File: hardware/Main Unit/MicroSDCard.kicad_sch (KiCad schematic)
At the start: 18 parts, among them J10 DM3AT, U7 74AHC1G04, U8 AP22913W6-7, U9 SN74AXC4T774

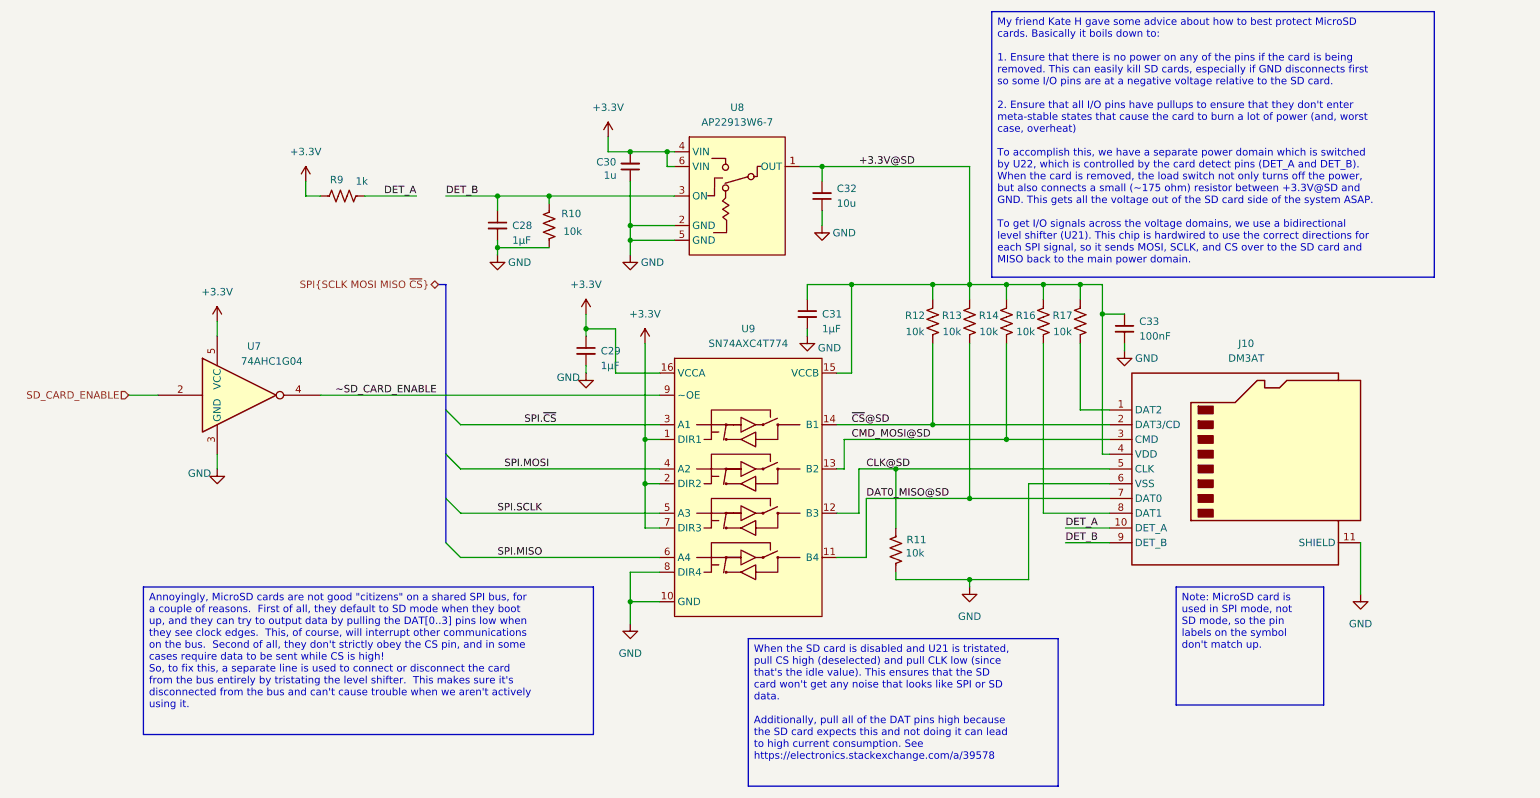
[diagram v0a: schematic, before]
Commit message: Implement Ethernet, start on voltage regulator
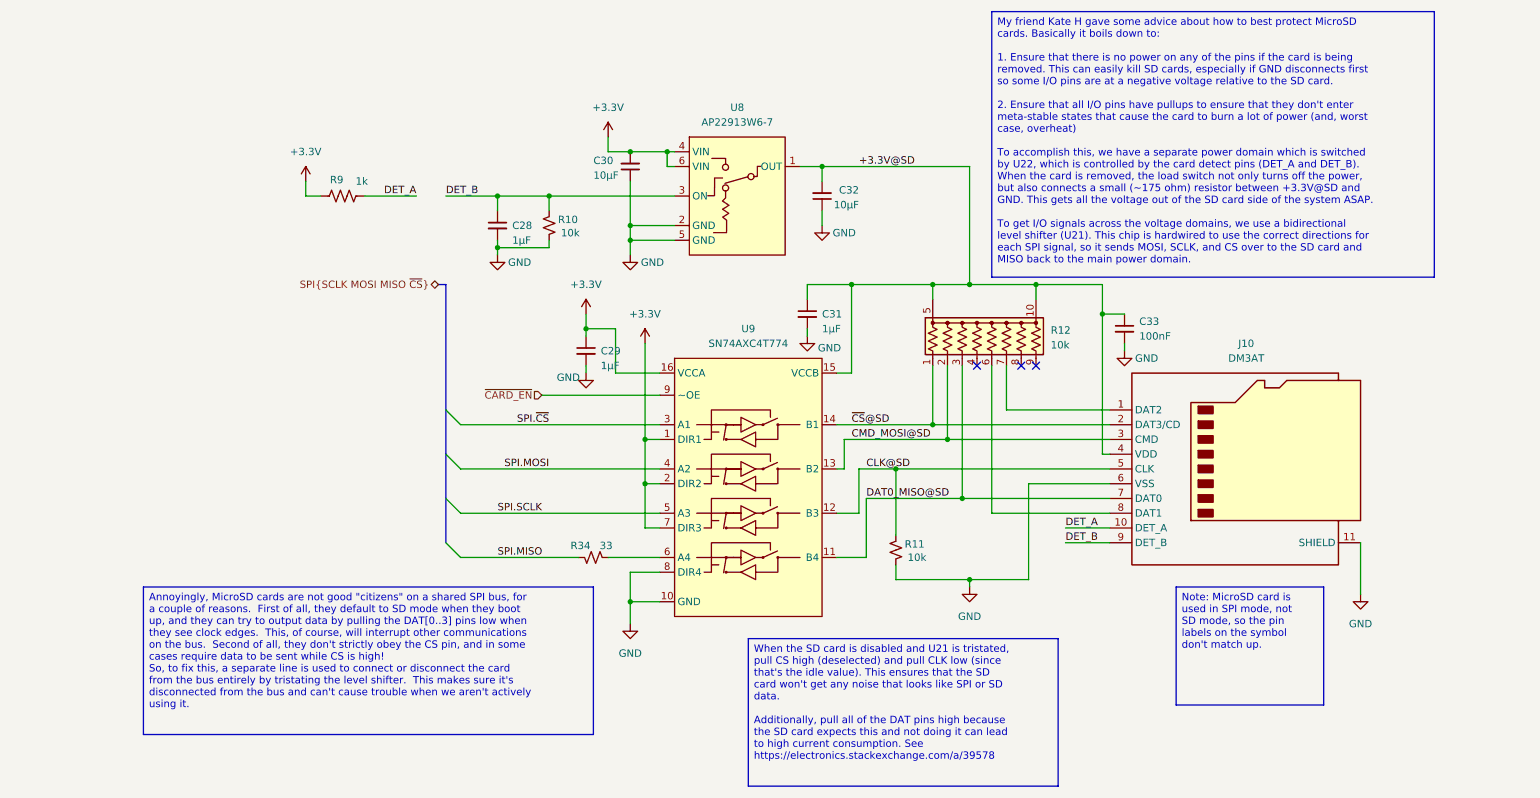
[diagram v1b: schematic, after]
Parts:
- removed R10, R11, R12, R13, R14, R16, R17: 10k, Resistor_SMD:R_1206_3216Metric, symbol Device:R_US
- removed U7: 74AHC1G04, Package_TO_SOT_SMD:SOT-23-5, symbol 74xGxx:74AHC1G04
- added R10, R11: 10k, Resistor_SMD:R_0603_1608Metric, symbol Device:R_Small_US
- added R12: 10k, Project Library:CTS 745C101, symbol Project Library:CTS 745C101
- added R34: 33, Resistor_SMD:R_0603_1608Metric, symbol Device:R_Small_US
- C30: value 1u -> 10µF; LibRef CL31B105KBHNNNE -> CL31B106KLHNNNE
- C32: value 10u -> 10µF
- U8: symbol project libraries:AP22913W6-7 -> Project Library:AP22913W6-7
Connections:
- net +3.3V@SD: now also R12.10 (common), R12.5 (common)
- net CLK@SD: now also R11.2
- net CMD_MOSI@SD: now also R12.2 (R2)
- net DAT0_MISO@SD: now also R12.3 (R3)
- net DET_B: now also R10.2
- net GND: now also R10.1, R11.1
- net SPI.MISO: now also R34.1; no longer U9.6 (A4)
- net ~{CS}@SD: now also R12.1 (R1)
- net at J10.8 (DAT1): now also R12.6 (R5)
- net at J10.1 (DAT2): now also R12.7 (R6)
- net ~SD_CARD_ENABLE renamed ~{CARD_EN}
- new net: R34.2, U9.6 (A4)
- no-connect marks 0 -> 3

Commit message: Main unit: Add USB port for MCU and 3.3VA rail, start on routing
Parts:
- U9: symbol project libraries:SN74AXC4T774 -> Project Library:SN74AXC4T774
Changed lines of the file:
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@@
 	)
 	(symbol
-		(lib_id "project libraries:SN74AXC4T774")
+		(lib_id "Project Library:SN74AXC4T774")
 		(at 140.97 93.98 0)
 		(unit 1)

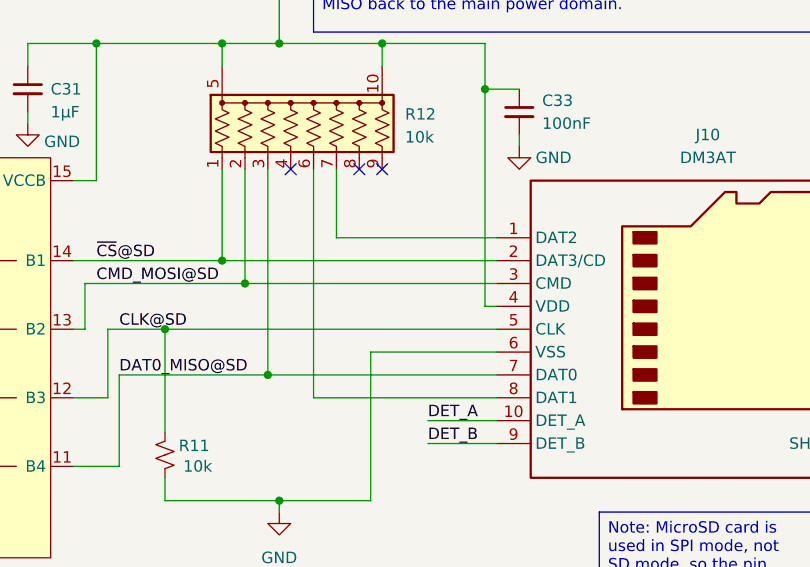
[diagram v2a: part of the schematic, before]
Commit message: Route most of the data lines on the PCB
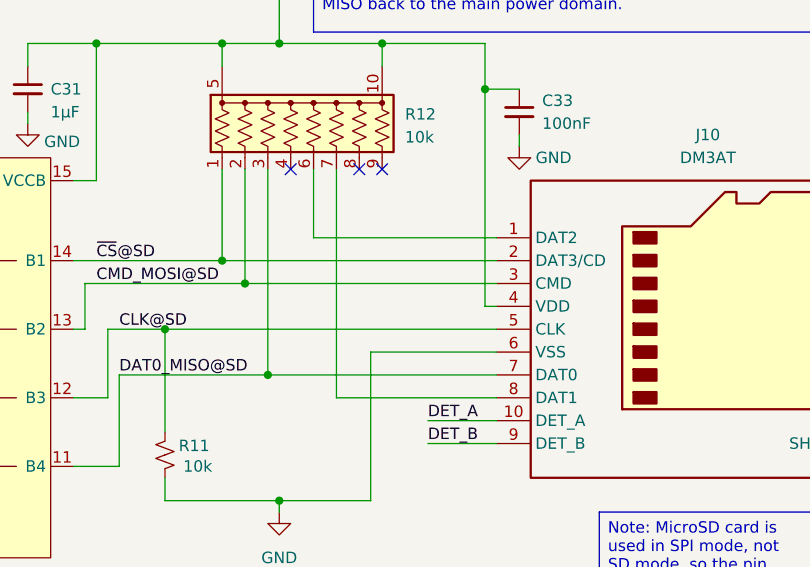
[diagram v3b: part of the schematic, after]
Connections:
- net at R12.6 (R5): now also J10.1 (DAT2); no longer J10.8 (DAT1)
- net at R12.7 (R6): now also J10.8 (DAT1); no longer J10.1 (DAT2)
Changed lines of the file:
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@@
-	(wire
-		(pts
-			(xy 182.88 101.6) (xy 203.2 101.6)
-		)
-		(stroke
-			(width 0)
-			(type default)
-		)
-	)
 	(wire
 		(pts
@@
 	(wire
 		(pts
+			(xy 185.42 76.2) (xy 185.42 101.6)
+		)
+		(stroke
+			(width 0)
+			(type default)
+		)
+	)
+	(wire
+		(pts
 			(xy 205.74 72.39) (xy 205.74 73.66)
 		)
@@
 	(wire
 		(pts
-			(xy 182.88 101.6) (xy 182.88 76.2)
-		)
-		(stroke
-			(width 0)
-			(type default)
-		)
-	)
-	(wire
-		(pts
-			(xy 185.42 83.82) (xy 203.2 83.82)
+			(xy 185.42 101.6) (xy 203.2 101.6)
 		)
 		(stroke
@@
 	(wire
 		(pts
+			(xy 182.88 83.82) (xy 203.2 83.82)
+		)
+		(stroke
+			(width 0)
+			(type default)
+		)
+	)
+	(wire
+		(pts
 			(xy 88.9 46.99) (xy 97.79 46.99)
 		)
@@
 	(wire
 		(pts
-			(xy 185.42 83.82) (xy 185.42 76.2)
-		)
-		(stroke
-			(width 0)
-			(type default)
-		)
-	)
-	(wire
-		(pts
 			(xy 123.19 96.52) (xy 123.19 88.9)
 		)
@@
 		)
 		(stroke
+			(width 0)
+			(type default)
+		)
+	)
+	(wire
+		(pts
+			(xy 182.88 76.2) (xy 182.88 83.82)
+		)
+		(stroke

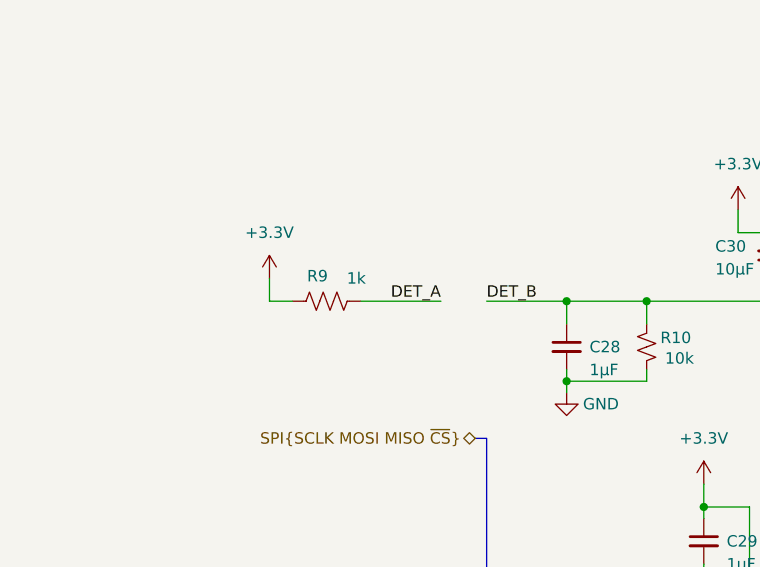
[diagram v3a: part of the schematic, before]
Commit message: Add schematic for Vsupply input
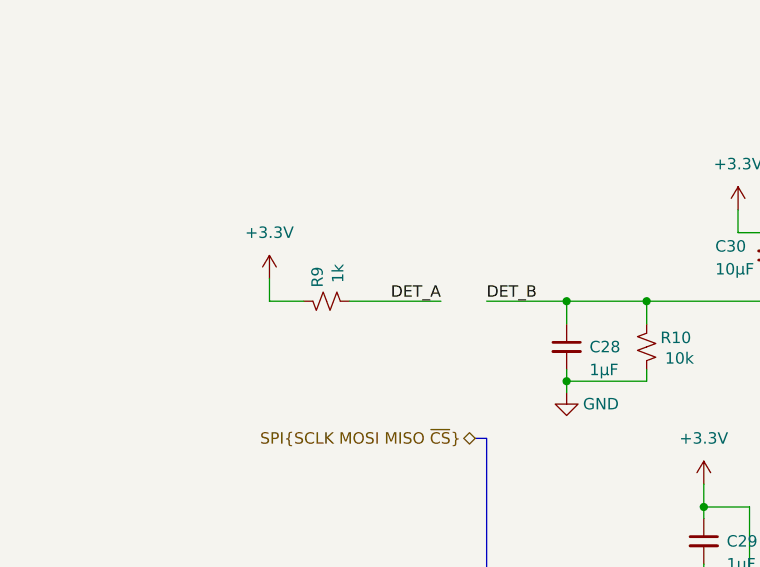
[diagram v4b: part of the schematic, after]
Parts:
- removed R9: 1k, Resistor_SMD:R_1206_3216Metric, symbol Device:R_US
- added R9: 1k, Resistor_SMD:R_0603_1608Metric, symbol Device:R_Small_US
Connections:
- net +3.3V: now also R9.2
- net DET_A: now also R9.1
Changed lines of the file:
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@@
 	(wire
 		(pts
-			(xy 67.31 46.99) (xy 64.77 46.99)
+			(xy 64.77 46.99) (xy 68.58 46.99)
 		)
 		(stroke
@@
 	(wire
 		(pts
+			(xy 73.66 46.99) (xy 83.82 46.99)
+		)
+		(stroke
+			(width 0)
+			(type default)
+		)
+	)
+	(wire
+		(pts
 			(xy 172.72 62.23) (xy 172.72 64.77)
 		)
@@
 		(pts
 			(xy 166.37 93.98) (xy 203.2 93.98)
-		)
-		(stroke
-			(width 0)
-			(type default)
-		)
-	)
-	(wire
-		(pts
-			(xy 74.93 46.99) (xy 83.82 46.99)
 		)
 		(stroke
@@
 			)
 			(justify right)
+		)
+	)
+	(symbol
+		(lib_id "Device:R_Small_US")
+		(at 71.12 46.99 270)
+		(mirror x)
+		(unit 1)
+		(exclude_from_sim no)
+		(in_bom yes)
+		(on_board yes)
+		(dnp no)
+		(property "Reference" "R9"
+			(at 70.104 45.466 0)
+			(effects
+				(font
+					(size 1.27 1.27)
+				)
+				(justify left)
+			)
+		)
+		(property "Value" "1k"
+			(at 72.39 44.958 0)
+			(effects
+				(font
+					(size 1.27 1.27)
+				)
+				(justify left)
+			)
+		)
+		(property "Footprint" "Resistor_SMD:R_0603_1608Metric"
+			(at 71.12 46.99 0)
+			(effects
+				(font
+					(size 1.27 1.27)
+				)
+				(hide yes)
+			)
+		)
+		(property "Datasheet" "~"
+			(at 71.12 46.99 0)
+			(effects
+				(font
+					(size 1.27 1.27)
+				)
+				(hide yes)
+			)
+		)
+		(property "Description" "Resistor, small US symbol"
+			(at 71.12 46.99 0)
+			(effects
+				(font
+					(size 1.27 1.27)
+				)
+				(hide yes)
+			)
+		)
+		(property "Supplier" "Digi-Key"
+			(at 71.12 46.99 0)
+			(effects
+				(font
+					(size 1.27 1.27)
+				)
+				(hide yes)
+			)
+		)
+		(property "SKU" "311-1.00KHRCT-ND"
+			(at 71.12 46.99 0)
+			(effects
+				(font
+					(size 1.27 1.27)
+				)
+				(hide yes)
+			)
+		)
+		(property "Mating Connector" ""
+			(at 71.12 46.99 0)
+			(effects
+				(font
+					(size 1.27 1.27)
+				)
+				(hide yes)
+			)
+		)
+		(property "LibRef" "RC0603FR-071KL"
+			(at 71.12 46.99 0)
+			(effects
+				(font
+					(size 1.27 1.27)
+				)
+				(hide yes)
+			)
+		)
+		(pin "2"
+		)
+		(pin "1"
+		)
+		(instances
+			(project "Main Unit"
+				(path "/7d91f165-331a-4c48-9d02-ee2a0aa7e94a/171a326f-5e68-4f6e-be23-ff3df57281ba"
+					(reference "R9")
+					(unit 1)
+				)
+			)
 		)
 	)
@@
 					(unit 1)
 				)
-			)
-		)
-	)
-	(symbol
-		(lib_id "Device:R_US")
-		(at 71.12 46.99 90)
-		(unit 1)
-		(exclude_from_sim no)
-		(in_bom yes)
-		(on_board yes)
-		(dnp no)
-		(property "Reference" "R9"
-			(at 70.104 44.196 90)
-			(effects
-				(font
-					(size 1.27 1.27)
-				)
-			)
-		)
-		(property "Value" "1k"
-			(at 74.422 44.45 90)
-			(effects
-				(font
-					(size 1.27 1.27)
-				)
-			)
-		)
-		(property "Footprint" "Resistor_SMD:R_1206_3216Metric"
-			(at 71.374 45.974 90)
-			(effects
-				(font
-					(size 1.27 1.27)
-				)
-				(hide yes)
-			)
-		)
-		(property "Datasheet" "~"
-			(at 71.12 46.99 0)
-			(effects
-				(font
-					(size 1.27 1.27)
-				)
-				(hide yes)
-			)
-		)
-		(property "Description" "Resistor, US symbol"
-			(at 71.12 46.99 0)
-			(effects
-				(font
-					(size 1.27 1.27)
-				)
-				(hide yes)
-			)
-		)
-		(property "Supplier" "Digi-Key"
-			(at 71.12 46.99 0)
-			(effects
-				(font
-					(size 1.27 1.27)
-				)
-				(hide yes)
-			)
-		)
-		(property "LibRef" "ERJ-8ENF1001V"
-			(at 71.12 46.99 0)
-			(effects
-				(font
-					(size 1.27 1.27)
-				)
-				(hide yes)
-			)
-		)
-		(property "SKU" "P1.00KFCT-ND"
-			(at 71.12 46.99 0)
-			(effects
-				(font
-					(size 1.27 1.27)
-				)
-				(hide yes)
-			)
-		)
-		(pin "1"
-		)
-		(pin "2"
-		)
-		(instances
-			(project "Main Unit"
-				(path "/7d91f165-331a-4c48-9d02-ee2a0aa7e94a/171a326f-5e68-4f6e-be23-ff3df57281ba"
-					(reference "R9")
-					(unit 1)
-				)

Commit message: Geographical reannotate
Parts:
- renumbered C33 to C38, C29 to C39, C31 to C41, C32 to C44, C28 to C45, C30 to C58, J10 to J14, R34 to R21, R12 to R24, R11 to R25, R10 to R28, R9 to R59, U8 to U13
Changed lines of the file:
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@@
 		(on_board yes)
 		(dnp no)
-		(property "Reference" "R9"
+		(property "Reference" "R59"
 			(at 70.104 45.466 0)
 			(effects
@@
 			(project "HackerDAQ Main Unit"
 				(path "/7d91f165-331a-4c48-9d02-ee2a0aa7e94a/171a326f-5e68-4f6e-be23-ff3df57281ba"
-					(reference "R9")
+					(reference "R59")
 					(unit 1)
 				)
@@
 		(dnp no)
 		(fields_autoplaced yes)
-		(property "Reference" "R12"
+		(property "Reference" "R24"
 			(at 193.04 70.1039 0)
 			(effects
@@
 			(project "HackerDAQ Main Unit"
 				(path "/7d91f165-331a-4c48-9d02-ee2a0aa7e94a/171a326f-5e68-4f6e-be23-ff3df57281ba"
-					(reference "R12")
+					(reference "R24")
 					(unit 1)
 				)
@@
 		(dnp no)
 		(fields_autoplaced yes)
-		(property "Reference" "U8"
+		(property "Reference" "U13"
 			(at 139.065 31.75 0)
 			(effects
@@
 			(project "HackerDAQ Main Unit"
 				(path "/7d91f165-331a-4c48-9d02-ee2a0aa7e94a/171a326f-5e68-4f6e-be23-ff3df57281ba"
-					(reference "U8")
+					(reference "U13")
 					(unit 1)
 				)
@@
 		(on_board yes)
 		(dnp no)
-		(property "Reference" "R11"
+		(property "Reference" "R25"
 			(at 167.894 106.934 0)
 			(effects
@@
 			(project "HackerDAQ Main Unit"
 				(path "/7d91f165-331a-4c48-9d02-ee2a0aa7e94a/171a326f-5e68-4f6e-be23-ff3df57281ba"
-					(reference "R11")
+					(reference "R25")
 					(unit 1)
 				)
@@
 		(on_board yes)
 		(dnp no)
-		(property "Reference" "R10"
+		(property "Reference" "R28"
 			(at 108.204 51.054 0)
 			(effects
@@
 			(project "HackerDAQ Main Unit"
 				(path "/7d91f165-331a-4c48-9d02-ee2a0aa7e94a/171a326f-5e68-4f6e-be23-ff3df57281ba"
-					(reference "R10")
+					(reference "R28")
 					(unit 1)
 				)
@@
 		(on_board yes)
 		(dnp no)
-		(property "Reference" "C31"
+		(property "Reference" "C41"
 			(at 153.67 67.3162 0)
 			(effects
@@
 			(project "HackerDAQ Main Unit"
 				(path "/7d91f165-331a-4c48-9d02-ee2a0aa7e94a/171a326f-5e68-4f6e-be23-ff3df57281ba"
-					(reference "C31")
+					(reference "C41")
 					(unit 1)
 				)
@@
 		(dnp no)
 		(fields_autoplaced yes)
-		(property "Reference" "J10"
+		(property "Reference" "J14"
 			(at 226.695 72.39 0)
 			(effects
@@
 			(project "HackerDAQ Main Unit"
 				(path "/7d91f165-331a-4c48-9d02-ee2a0aa7e94a/171a326f-5e68-4f6e-be23-ff3df57281ba"
-					(reference "J10")
+					(reference "J14")
 					(unit 1)
 				)
@@
 		(on_board yes)
 		(dnp no)
-		(property "Reference" "C29"
+		(property "Reference" "C39"
 			(at 115.57 73.6662 0)
 			(effects
@@
 			(project "HackerDAQ Main Unit"
 				(path "/7d91f165-331a-4c48-9d02-ee2a0aa7e94a/171a326f-5e68-4f6e-be23-ff3df57281ba"
-					(reference "C29")
+					(reference "C39")
 					(unit 1)
 				)
@@
 		(on_board yes)
 		(dnp no)
-		(property "Reference" "C32"
+		(property "Reference" "C44"
 			(at 160.02 45.974 0)
 			(effects
@@
 			(project "HackerDAQ Main Unit"
 				(path "/7d91f165-331a-4c48-9d02-ee2a0aa7e94a/171a326f-5e68-4f6e-be23-ff3df57281ba"
-					(reference "C32")
+					(reference "C44")
 					(unit 1)
 				)
@@
 		(on_board yes)
 		(dnp no)
-		(property "Reference" "R34"
+		(property "Reference" "R21"
 			(at 113.792 107.188 90)
 			(effects
@@
 			(project "HackerDAQ Main Unit"
 				(path "/7d91f165-331a-4c48-9d02-ee2a0aa7e94a/171a326f-5e68-4f6e-be23-ff3df57281ba"
-					(reference "R34")
+					(reference "R21")
 					(unit 1)
 				)
@@
 		(on_board yes)
 		(dnp no)
-		(property "Reference" "C30"
+		(property "Reference" "C58"
 			(at 114.3 40.894 0)
 			(effects
@@
 			(project "HackerDAQ Main Unit"
 				(path "/7d91f165-331a-4c48-9d02-ee2a0aa7e94a/171a326f-5e68-4f6e-be23-ff3df57281ba"
-					(reference "C30")
+					(reference "C58")
 					(unit 1)
 				)
@@
 		(dnp no)
 		(fields_autoplaced yes)
-		(property "Reference" "C33"
+		(property "Reference" "C38"
 			(at 208.28 68.5862 0)
 			(effects
@@
 			(project "HackerDAQ Main Unit"
 				(path "/7d91f165-331a-4c48-9d02-ee2a0aa7e94a/171a326f-5e68-4f6e-be23-ff3df57281ba"
-					(reference "C33")
+					(reference "C38")
 					(unit 1)
 				)
@@
 		(on_board yes)
 		(dnp no)
-		(property "Reference" "C28"
+		(property "Reference" "C45"
 			(at 100.33 52.0762 0)
 			(effects
@@
 			(project "HackerDAQ Main Unit"
 				(path "/7d91f165-331a-4c48-9d02-ee2a0aa7e94a/171a326f-5e68-4f6e-be23-ff3df57281ba"
-					(reference "C28")
-					(unit 1)
-				)
+					(reference "C45")
+					(unit 1)
+				)
